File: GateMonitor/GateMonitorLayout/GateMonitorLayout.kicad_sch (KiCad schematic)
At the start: 25 parts, among them J1 Screw_Terminal_01x03, J2 PIR sensor, J3 Conn_01x03, J4 Hall effect, Q1 IRLB8721PBF, U1 Ra01_Breakout_Module, U2 MIC2954, U3 PICAXE-14M2

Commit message: Gate monitor layout mostly done
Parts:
- removed F1: 250mA, Custom:Fuseholder5x20_horiz_open_lateral_Type-II, symbol Device:Fuse
- removed U3: PICAXE-14M2, Package_DIP:DIP-14_W7.62mm_Socket_LongPads, symbol picaxe-3:PICAXE-14M2
- added J4: AHT20 temperature sensor, Connector_PinSocket_2.54mm:PinSocket_1x04_P2.54mm_Vertical, symbol Connector:Conn_01x04_Socket
- added R11: 4.7k, Resistor_THT:R_Axial_DIN0207_L6.3mm_D2.5mm_P7.62mm_Horizontal, symbol Device:R
- added R8: 4.7k, Resistor_THT:R_Axial_DIN0207_L6.3mm_D2.5mm_P5.08mm_Vertical, symbol Device:R
- added U2: PICAXE-18M2, Package_DIP:DIP-18_W7.62mm_Socket_LongPads, symbol picaxe-3:PICAXE-18M2
- C1: footprint Capacitor_THT:CP_Radial_D6.3mm_P2.50mm -> Capacitor_THT:C_Rect_L13.0mm_W6.0mm_P10.00mm_FKS3_FKP3_MKS4
- C2: footprint Capacitor_THT:C_Disc_D3.0mm_W1.6mm_P2.50mm -> Capacitor_THT:C_Disc_D7.0mm_W2.5mm_P5.00mm
- C3: renamed from C4; footprint Capacitor_THT:CP_Radial_D6.3mm_P2.50mm -> Capacitor_THT:CP_Radial_D8.0mm_P5.00mm
- C4: renamed from C3; footprint Capacitor_THT:C_Disc_D3.0mm_W1.6mm_P2.50mm -> Capacitor_THT:C_Axial_L3.8mm_D2.6mm_P12.50mm_Horizontal
- D1, D2: footprint Diode_THT:D_DO-41_SOD81_P10.16mm_Horizontal -> Diode_THT:D_DO-41_SOD81_P5.08mm_Vertical_AnodeUp
- R10: renamed from R7; footprint OptoDevice:R_LDR_5.1x4.3mm_P3.4mm_Vertical -> OptoDevice:R_LDR_7x6mm_P5.1mm_Vertical
- R2: renamed from R1; footprint Resistor_THT:R_Axial_DIN0207_L6.3mm_D2.5mm_P10.16mm_Horizontal -> Resistor_THT:R_Axial_DIN0207_L6.3mm_D2.5mm_P5.08mm_Vertical
- R3: renamed from R2; footprint Resistor_THT:R_Axial_DIN0207_L6.3mm_D2.5mm_P10.16mm_Horizontal -> Resistor_THT:R_Axial_DIN0207_L6.3mm_D2.5mm_P5.08mm_Vertical
- R6: renamed from R8; footprint Resistor_THT:R_Axial_DIN0207_L6.3mm_D2.5mm_P10.16mm_Horizontal -> Resistor_THT:R_Axial_DIN0207_L6.3mm_D2.5mm_P5.08mm_Vertical
- R7: renamed from R9; footprint Resistor_THT:R_Axial_DIN0207_L6.3mm_D2.5mm_P10.16mm_Horizontal -> Resistor_THT:R_Axial_DIN0204_L3.6mm_D1.6mm_P2.54mm_Vertical
- renumbered J3 to J2, J2 to J3, J4 to J5, R4 to R1, R3 to R4, R6 to R9, U2 to U3
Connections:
- net +3.3V: now also J5.3 (Pin_3), J4.1 (Pin_1), R11.1, R8.1, U2.14 (VDD)
- net +BATT: now also D1.1 (K), J1.1 (Pin_1); no longer J5.1 (Pin_1)
- net GNDREF: now also J1.3 (Pin_3), J5.1 (Pin_1), J4.2 (Pin_2), U2.5 (VSS); no longer J1.1 (Pin_1), J5.3 (Pin_3)
- net at J2.2 (Pin_2), R1.1: now also R2.2; no longer R2.1
- net at J2.3 (Pin_3): now also U2.2 (C.3/TX); no longer R5.1
- net Aux power: now reaches Q1.1 (G)
- net Aux power: now also U2.12 (B.6)
- net PIR: now reaches J3.2 (Pin_2)
- net PIR: now also U2.15 (C.6); no longer R2.2
- net Battery ADC: now reaches R6.2, R7.1
- net Battery ADC: now also U2.1 (C.2)
- net LDR ADC: now reaches R10.1, R9.2
- net LDR ADC: now also U2.18 (C.1)
- net Hall effect: now reaches J5.2 (Pin_2)
- net Hall effect: now also U2.17 (C.0)
- net at U1.6 (MOSI): now also U2.6 (B.0)
- net at U1.5 (DIO0): now also U2.4 (C.5)
- net at U1.4 (MISO): now also U2.11 (B.5)
- net at U1.3 (SCK): now also U2.8 (B.2)
- net at U1.2 (RST): now also U2.9 (B.3)
- net at U1.7 (NSS): now also U2.13 (B.7)
- new net: R2.1, U2.3 (C.4/RX)
- new net I2C SCL: J4.3 (Pin_3), R8.2, U2.10 (B.4)
- new net I2C SDA: J4.4 (Pin_4), R11.2, U2.7 (B.1)
- new net LED: R5.1, U2.16 (C.7)
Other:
- moved on the sheet: C1, C2, C3, C4, D1, D2, D3, J1, J2, J3, J5, Q1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

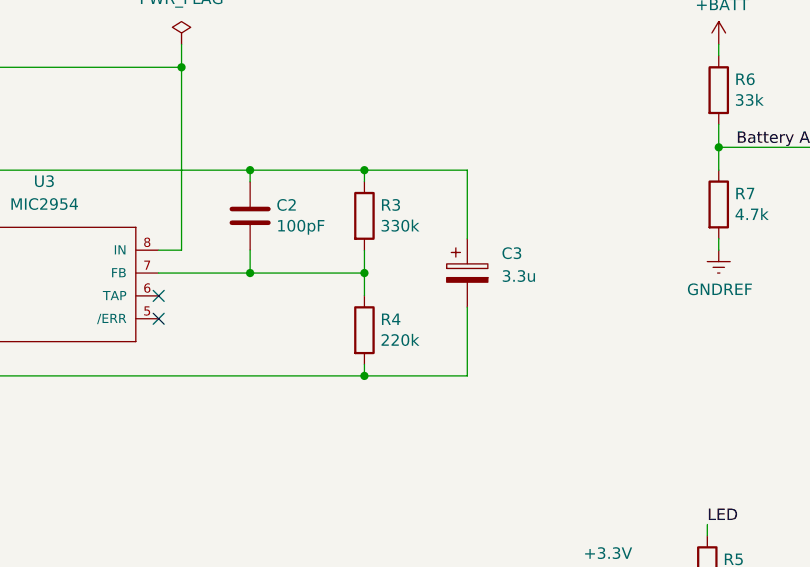
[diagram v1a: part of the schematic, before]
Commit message: Added holes and grid to gate monitor layout
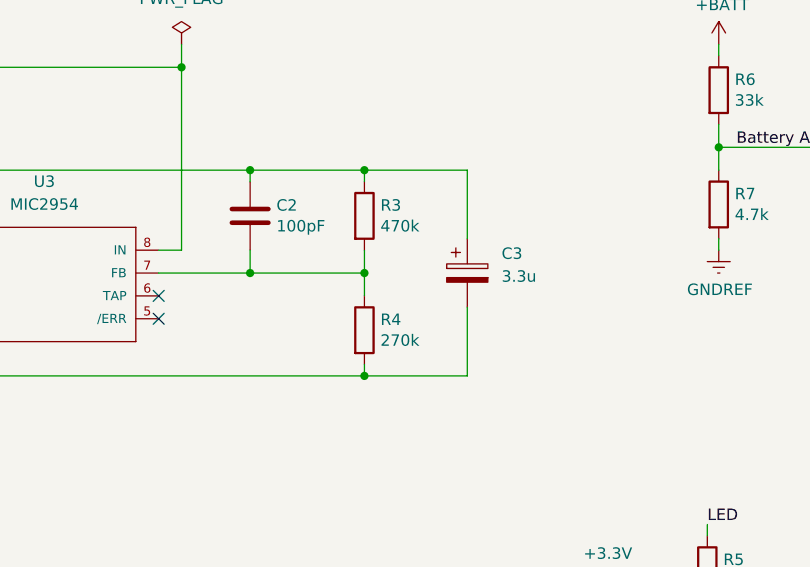
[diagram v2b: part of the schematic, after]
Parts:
- R3: value 330k -> 470k
- R4: value 220k -> 270k
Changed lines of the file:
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@@
 			)
 		)
-		(property "Value" "330k"
+		(property "Value" "470k"
 			(at 155.448 54.483 0)
 			(effects
@@
 			)
 		)
-		(property "Value" "220k"
+		(property "Value" "270k"
 			(at 155.448 67.183 0)
 			(effects
